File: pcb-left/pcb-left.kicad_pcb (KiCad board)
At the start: 2 copper layers, 124.8 x 104.5 mm, 43 parts, among them J1 BAT, U1 xiao-ble

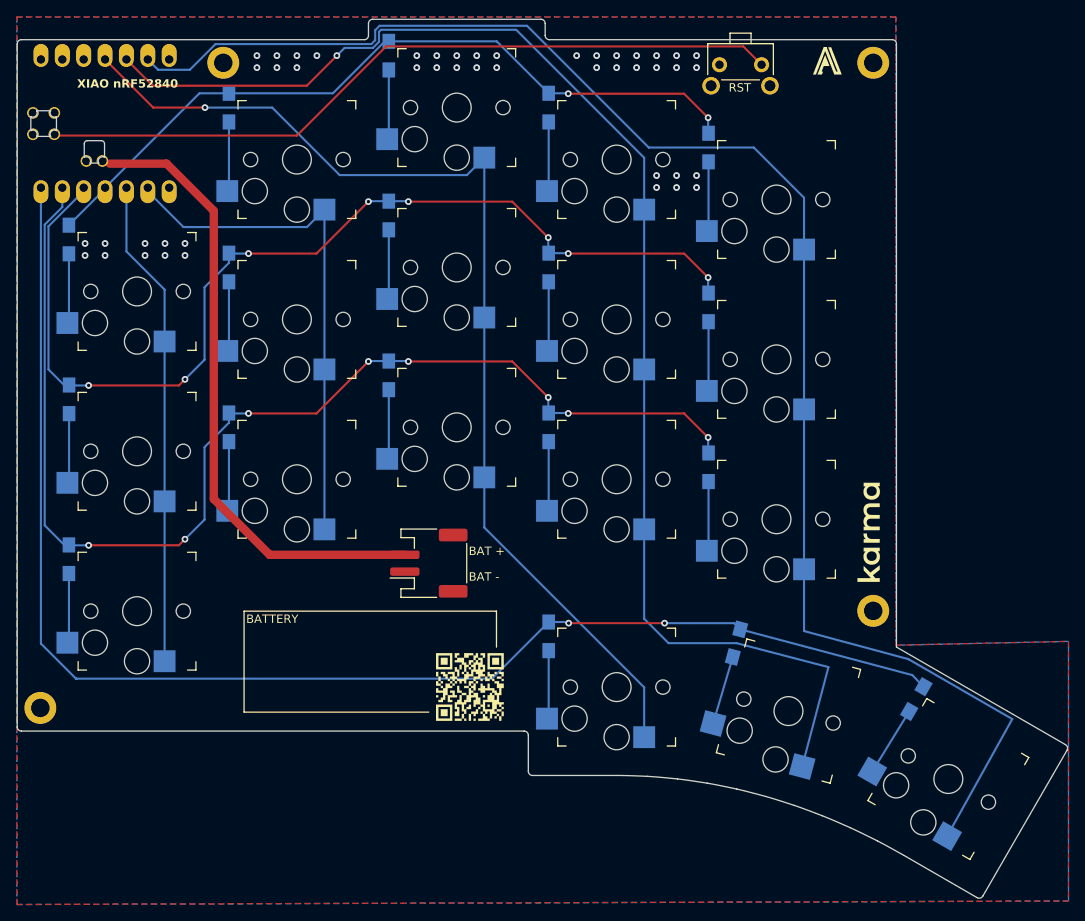
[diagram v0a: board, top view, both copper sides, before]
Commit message: support kailh choc v2
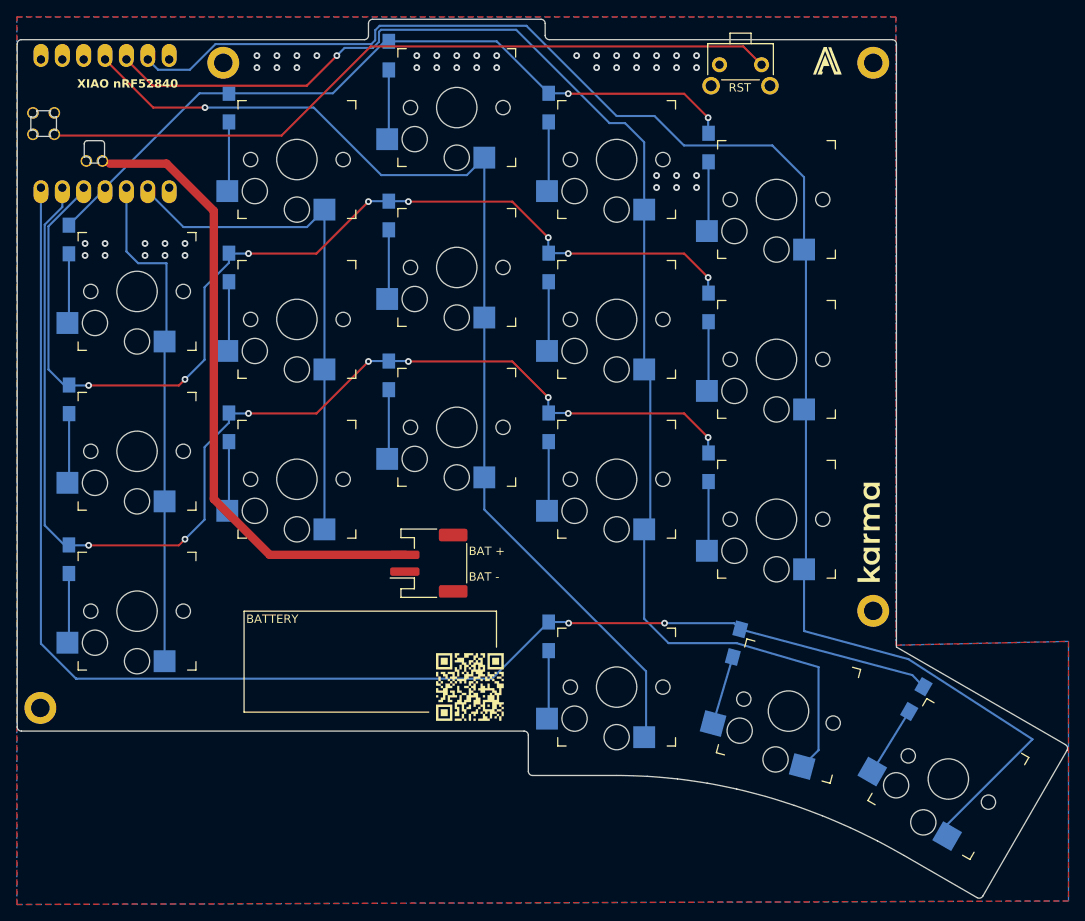
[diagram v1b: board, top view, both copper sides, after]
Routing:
- net COL4_L: track 184.3 -> 189.2 mm
- net COL0_L: track 58.2 -> 60.3 mm
- net COL3_L: track 163.1 -> 164.0 mm
